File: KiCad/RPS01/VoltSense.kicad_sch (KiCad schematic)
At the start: 0 parts

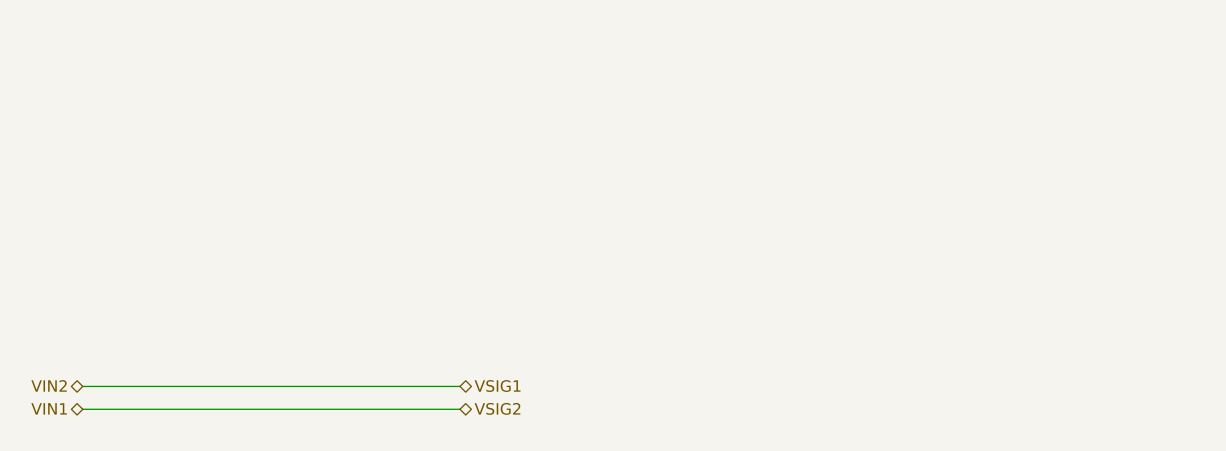
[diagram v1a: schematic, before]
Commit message: Finished most of the Schematics. Needs polishing
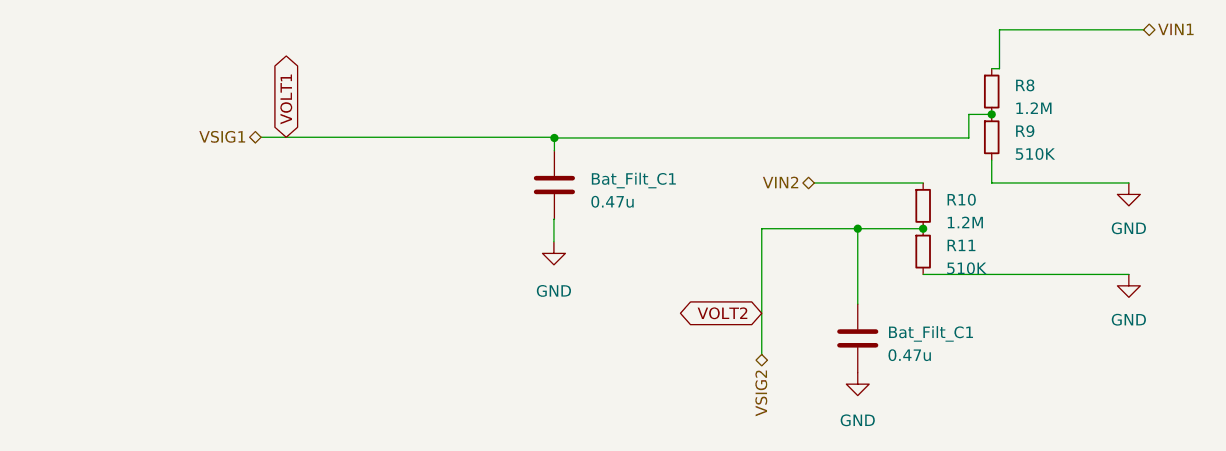
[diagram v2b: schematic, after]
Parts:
- added Bat_Filt_C1 (x2): 0.47u, symbol Device:C
- added R10, R8: 1.2M, Resistor_SMD:R_1206_3216Metric, symbol Device:R_Small
- added R11, R9: 510K, Resistor_SMD:R_1206_3216Metric, symbol Device:R_Small
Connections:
- net VIN1: now also R8.1
- net VIN2: now also R10.1
- new net GND: Bat_Filt_C1.2, Bat_Filt_C1.2, R11.2, R9.2
- new net VOLT1: Bat_Filt_C1.1, R8.2, R9.1
- new net VOLT2: Bat_Filt_C1.1, R10.2, R11.1

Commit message: Finished Updating Footprints and Reorganized Reference Designators
Finished Updating Footprints and Reorganized Reference Designators

Starting to work on Final PCB, except for 19V Boost. Please check Schematic for errors
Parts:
- Bat_Filt_C? (x2): renamed from Bat_Filt_C1; footprint (none) -> Capacitor_SMD:C_0603_1608Metric
- renumbered R9 to R?, R10 to R?, R8 to R?, R11 to R?
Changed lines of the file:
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@@
   (symbol (lib_id "Device:R_Small") (at 183.0324 49.784 0) (unit 1)
     (in_bom yes) (on_board yes) (dnp no) (fields_autoplaced)
-    (property "Reference" "R9" (at 185.5724 49.149 0)
+    (property "Reference" "R?" (at 185.5724 49.149 0)
       (effects (font (size 1.27 1.27)) (justify left))
     )
@@
       (project "rps01"
         (path "/14930f15-c0a0-4b55-93e6-b112548415f6/a2e49fe6-126d-427d-b045-54fb7f662aa7"
-          (reference "R9") (unit 1)
-        )
-        (path "/14930f15-c0a0-4b55-93e6-b112548415f6/86aa0a4b-8e23-451d-9b8a-c1446d1d5d38"
-          (reference "R23") (unit 1)
+          (reference "R?") (unit 1)
+        )
+        (path "/14930f15-c0a0-4b55-93e6-b112548415f6/86aa0a4b-8e23-451d-9b8a-c1446d1d5d38"
+          (reference "R28") (unit 1)
         )
       )
@@
   (symbol (lib_id "power:GND") (at 134.3914 61.4172 0) (unit 1)
     (in_bom yes) (on_board yes) (dnp no) (fields_autoplaced)
-    (property "Reference" "#PWR038" (at 134.3914 67.7672 0)
+    (property "Reference" "#PWR?" (at 134.3914 67.7672 0)
       (effects (font (size 1.27 1.27)) hide)
     )
@@
       (project "rps01"
         (path "/14930f15-c0a0-4b55-93e6-b112548415f6/a2e49fe6-126d-427d-b045-54fb7f662aa7"
-          (reference "#PWR038") (unit 1)
-        )
-        (path "/14930f15-c0a0-4b55-93e6-b112548415f6/86aa0a4b-8e23-451d-9b8a-c1446d1d5d38"
-          (reference "#PWR045") (unit 1)
+          (reference "#PWR?") (unit 1)
+        )
+        (path "/14930f15-c0a0-4b55-93e6-b112548415f6/86aa0a4b-8e23-451d-9b8a-c1446d1d5d38"
+          (reference "#PWR047") (unit 1)
         )
       )
@@
   (symbol (lib_id "power:GND") (at 168.148 75.946 0) (unit 1)
     (in_bom yes) (on_board yes) (dnp no) (fields_autoplaced)
-    (property "Reference" "#PWR046" (at 168.148 82.296 0)
+    (property "Reference" "#PWR048" (at 168.148 82.296 0)
       (effects (font (size 1.27 1.27)) hide)
     )
@@
       (project "rps01"
         (path "/14930f15-c0a0-4b55-93e6-b112548415f6/86aa0a4b-8e23-451d-9b8a-c1446d1d5d38"
-          (reference "#PWR046") (unit 1)
+          (reference "#PWR048") (unit 1)
         )
       )
@@
   (symbol (lib_id "Device:R_Small") (at 175.4124 57.404 0) (unit 1)
     (in_bom yes) (on_board yes) (dnp no) (fields_autoplaced)
-    (property "Reference" "R10" (at 177.9524 56.769 0)
+    (property "Reference" "R?" (at 177.9524 56.769 0)
       (effects (font (size 1.27 1.27)) (justify left))
     )
@@
       (project "rps01"
         (path "/14930f15-c0a0-4b55-93e6-b112548415f6/a2e49fe6-126d-427d-b045-54fb7f662aa7"
-          (reference "R10") (unit 1)
-        )
-        (path "/14930f15-c0a0-4b55-93e6-b112548415f6/86aa0a4b-8e23-451d-9b8a-c1446d1d5d38"
-          (reference "R20") (unit 1)
+          (reference "R?") (unit 1)
+        )
+        (path "/14930f15-c0a0-4b55-93e6-b112548415f6/86aa0a4b-8e23-451d-9b8a-c1446d1d5d38"
+          (reference "R25") (unit 1)
         )
       )
@@
   (symbol (lib_id "power:GND") (at 198.2724 54.864 0) (unit 1)
     (in_bom yes) (on_board yes) (dnp no) (fields_autoplaced)
-    (property "Reference" "#PWR019" (at 198.2724 61.214 0)
+    (property "Reference" "#PWR?" (at 198.2724 61.214 0)
       (effects (font (size 1.27 1.27)) hide)
     )
@@
       (project "rps01"
         (path "/14930f15-c0a0-4b55-93e6-b112548415f6/a2e49fe6-126d-427d-b045-54fb7f662aa7"
-          (reference "#PWR019") (unit 1)
-        )
-        (path "/14930f15-c0a0-4b55-93e6-b112548415f6/86aa0a4b-8e23-451d-9b8a-c1446d1d5d38"
-          (reference "#PWR047") (unit 1)
+          (reference "#PWR?") (unit 1)
+        )
+        (path "/14930f15-c0a0-4b55-93e6-b112548415f6/86aa0a4b-8e23-451d-9b8a-c1446d1d5d38"
+          (reference "#PWR049") (unit 1)
         )
       )
@@
   (symbol (lib_id "Device:C") (at 168.148 72.136 0) (unit 1)
     (in_bom yes) (on_board yes) (dnp no) (fields_autoplaced)
-    (property "Reference" "Bat_Filt_C1" (at 171.45 71.501 0)
+    (property "Reference" "Bat_Filt_C?" (at 171.45 71.501 0)
       (effects (font (size 1.27 1.27)) (justify left))
     )
@@
       (effects (font (size 1.27 1.27)) (justify left))
     )
-    (property "Footprint" "" (at 169.1132 75.946 0)
+    (property "Footprint" "Capacitor_SMD:C_0603_1608Metric" (at 169.1132 75.946 0)
       (effects (font (size 1.27 1.27)) hide)
     )
@@
       (project "rps01"
         (path "/14930f15-c0a0-4b55-93e6-b112548415f6/a2e49fe6-126d-427d-b045-54fb7f662aa7"
-          (reference "Bat_Filt_C1") (unit 1)
-        )
-        (path "/14930f15-c0a0-4b55-93e6-b112548415f6/86aa0a4b-8e23-451d-9b8a-c1446d1d5d38"
-          (reference "C9") (unit 1)
+          (reference "Bat_Filt_C?") (unit 1)
+        )
+        (path "/14930f15-c0a0-4b55-93e6-b112548415f6/86aa0a4b-8e23-451d-9b8a-c1446d1d5d38"
+          (reference "C12") (unit 1)
         )
       )
@@
   (symbol (lib_id "Device:C") (at 134.4422 55.0926 0) (unit 1)
     (in_bom yes) (on_board yes) (dnp no) (fields_autoplaced)
-    (property "Reference" "Bat_Filt_C1" (at 138.43 54.4576 0)
+    (property "Reference" "Bat_Filt_C?" (at 138.43 54.4576 0)
       (effects (font (size 1.27 1.27)) (justify left))
     )
@@
       (effects (font (size 1.27 1.27)) (justify left))
     )
-    (property "Footprint" "" (at 135.4074 58.9026 0)
+    (property "Footprint" "Capacitor_SMD:C_0603_1608Metric" (at 135.4074 58.9026 0)
       (effects (font (size 1.27 1.27)) hide)
     )
@@
       (project "rps01"
         (path "/14930f15-c0a0-4b55-93e6-b112548415f6/a2e49fe6-126d-427d-b045-54fb7f662aa7"
-          (reference "Bat_Filt_C1") (unit 1)
-        )
-        (path "/14930f15-c0a0-4b55-93e6-b112548415f6/86aa0a4b-8e23-451d-9b8a-c1446d1d5d38"
-          (reference "C8") (unit 1)
+          (reference "Bat_Filt_C?") (unit 1)
+        )
+        (path "/14930f15-c0a0-4b55-93e6-b112548415f6/86aa0a4b-8e23-451d-9b8a-c1446d1d5d38"
+          (reference "C11") (unit 1)
         )
       )
@@
   (symbol (lib_id "power:GND") (at 198.2724 65.024 0) (unit 1)
     (in_bom yes) (on_board yes) (dnp no) (fields_autoplaced)
-    (property "Reference" "#PWR024" (at 198.2724 71.374 0)
+    (property "Reference" "#PWR?" (at 198.2724 71.374 0)
       (effects (font (size 1.27 1.27)) hide)
     )
@@
       (project "rps01"
         (path "/14930f15-c0a0-4b55-93e6-b112548415f6/a2e49fe6-126d-427d-b045-54fb7f662aa7"
-          (reference "#PWR024") (unit 1)
-        )
-        (path "/14930f15-c0a0-4b55-93e6-b112548415f6/86aa0a4b-8e23-451d-9b8a-c1446d1d5d38"
-          (reference "#PWR048") (unit 1)
+          (reference "#PWR?") (unit 1)
+        )
+        (path "/14930f15-c0a0-4b55-93e6-b112548415f6/86aa0a4b-8e23-451d-9b8a-c1446d1d5d38"
+          (reference "#PWR050") (unit 1)
         )
       )
@@
   (symbol (lib_id "Device:R_Small") (at 183.0324 44.704 0) (unit 1)
     (in_bom yes) (on_board yes) (dnp no) (fields_autoplaced)
-    (property "Reference" "R8" (at 185.5724 44.069 0)
+    (property "Reference" "R?" (at 185.5724 44.069 0)
       (effects (font (size 1.27 1.27)) (justify left))
     )
@@
       (project "rps01"
         (path "/14930f15-c0a0-4b55-93e6-b112548415f6/a2e49fe6-126d-427d-b045-54fb7f662aa7"
-          (reference "R8") (unit 1)
-        )
-        (path "/14930f15-c0a0-4b55-93e6-b112548415f6/86aa0a4b-8e23-451d-9b8a-c1446d1d5d38"
-          (reference "R22") (unit 1)
+          (reference "R?") (unit 1)
+        )
+        (path "/14930f15-c0a0-4b55-93e6-b112548415f6/86aa0a4b-8e23-451d-9b8a-c1446d1d5d38"
+          (reference "R27") (unit 1)
         )
       )
@@
   (symbol (lib_id "Device:R_Small") (at 175.4124 62.484 0) (unit 1)
     (in_bom yes) (on_board yes) (dnp no) (fields_autoplaced)
-    (property "Reference" "R11" (at 177.9524 61.849 0)
+    (property "Reference" "R?" (at 177.9524 61.849 0)
       (effects (font (size 1.27 1.27)) (justify left))
     )
@@
       (project "rps01"
         (path "/14930f15-c0a0-4b55-93e6-b112548415f6/a2e49fe6-126d-427d-b045-54fb7f662aa7"
-          (reference "R11") (unit 1)
-        )
-        (path "/14930f15-c0a0-4b55-93e6-b112548415f6/86aa0a4b-8e23-451d-9b8a-c1446d1d5d38"
-          (reference "R21") (unit 1)
-        )
-      )
+          (reference "R?") (unit 1)
+        )
+        (path "/14930f15-c0a0-4b55-93e6-b112548415f6/86aa0a4b-8e23-451d-9b8a-c1446d1d5d38"
+          (reference "R26") (unit 1)
+        )
+      )

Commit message: Board Ready For layout. Except for 19V Boost? CHECK vs SIM Please
Board Ready For layout. Except for 19V Boost? CHECK vs SIM Please
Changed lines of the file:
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@@
   (symbol (lib_id "Device:R_Small") (at 183.0324 49.784 0) (unit 1)
     (in_bom yes) (on_board yes) (dnp no) (fields_autoplaced)
-    (property "Reference" "R?" (at 185.5724 49.149 0)
-      (effects (font (size 1.27 1.27)) (justify left))
-    )
-    (property "Value" "510K" (at 185.5724 51.689 0)
+    (property "Reference" "R?" (at 185.42 49.149 0)
+      (effects (font (size 1.27 1.27)) (justify left))
+    )
+    (property "Value" "510K" (at 185.42 51.689 0)
       (effects (font (size 1.27 1.27)) (justify left))
     )
@@
         )
         (path "/14930f15-c0a0-4b55-93e6-b112548415f6/86aa0a4b-8e23-451d-9b8a-c1446d1d5d38"
-          (reference "R28") (unit 1)
+          (reference "R_P8") (unit 1)
         )
       )
@@
         )
         (path "/14930f15-c0a0-4b55-93e6-b112548415f6/86aa0a4b-8e23-451d-9b8a-c1446d1d5d38"
-          (reference "#PWR047") (unit 1)
+          (reference "#PWR073") (unit 1)
         )
       )
@@
   (symbol (lib_id "power:GND") (at 168.148 75.946 0) (unit 1)
     (in_bom yes) (on_board yes) (dnp no) (fields_autoplaced)
-    (property "Reference" "#PWR048" (at 168.148 82.296 0)
+    (property "Reference" "#PWR075" (at 168.148 82.296 0)
       (effects (font (size 1.27 1.27)) hide)
     )
@@
       (project "rps01"
         (path "/14930f15-c0a0-4b55-93e6-b112548415f6/86aa0a4b-8e23-451d-9b8a-c1446d1d5d38"
-          (reference "#PWR048") (unit 1)
+          (reference "#PWR075") (unit 1)
         )
       )
@@
   (symbol (lib_id "Device:R_Small") (at 175.4124 57.404 0) (unit 1)
     (in_bom yes) (on_board yes) (dnp no) (fields_autoplaced)
-    (property "Reference" "R?" (at 177.9524 56.769 0)
-      (effects (font (size 1.27 1.27)) (justify left))
-    )
-    (property "Value" "1.2M" (at 177.9524 59.309 0)
+    (property "Reference" "R?" (at 177.8 56.769 0)
+      (effects (font (size 1.27 1.27)) (justify left))
+    )
+    (property "Value" "1.2M" (at 177.8 59.309 0)
       (effects (font (size 1.27 1.27)) (justify left))
     )
@@
         )
         (path "/14930f15-c0a0-4b55-93e6-b112548415f6/86aa0a4b-8e23-451d-9b8a-c1446d1d5d38"
-          (reference "R25") (unit 1)
+          (reference "R_P9") (unit 1)
         )
       )
@@
         )
         (path "/14930f15-c0a0-4b55-93e6-b112548415f6/86aa0a4b-8e23-451d-9b8a-c1446d1d5d38"
-          (reference "#PWR049") (unit 1)
+          (reference "#PWR072") (unit 1)
         )
       )
@@
         )
         (path "/14930f15-c0a0-4b55-93e6-b112548415f6/86aa0a4b-8e23-451d-9b8a-c1446d1d5d38"
-          (reference "C12") (unit 1)
+          (reference "C21") (unit 1)
         )
       )
@@
         )
         (path "/14930f15-c0a0-4b55-93e6-b112548415f6/86aa0a4b-8e23-451d-9b8a-c1446d1d5d38"
-          (reference "C11") (unit 1)
+          (reference "C20") (unit 1)
         )
       )
@@
         )
         (path "/14930f15-c0a0-4b55-93e6-b112548415f6/86aa0a4b-8e23-451d-9b8a-c1446d1d5d38"
-          (reference "#PWR050") (unit 1)
+          (reference "#PWR074") (unit 1)
         )
       )
@@
   (symbol (lib_id "Device:R_Small") (at 183.0324 44.704 0) (unit 1)
     (in_bom yes) (on_board yes) (dnp no) (fields_autoplaced)
-    (property "Reference" "R?" (at 185.5724 44.069 0)
-      (effects (font (size 1.27 1.27)) (justify left))
-    )
-    (property "Value" "1.2M" (at 185.5724 46.609 0)
+    (property "Reference" "R?" (at 185.42 44.069 0)
+      (effects (font (size 1.27 1.27)) (justify left))
+    )
+    (property "Value" "1.2M" (at 185.42 46.609 0)
       (effects (font (size 1.27 1.27)) (justify left))
     )
@@
         )
         (path "/14930f15-c0a0-4b55-93e6-b112548415f6/86aa0a4b-8e23-451d-9b8a-c1446d1d5d38"
-          (reference "R27") (unit 1)
+          (reference "R_P7") (unit 1)
         )
       )
@@
   (symbol (lib_id "Device:R_Small") (at 175.4124 62.484 0) (unit 1)
     (in_bom yes) (on_board yes) (dnp no) (fields_autoplaced)
-    (property "Reference" "R?" (at 177.9524 61.849 0)
-      (effects (font (size 1.27 1.27)) (justify left))
-    )
-    (property "Value" "510K" (at 177.9524 64.389 0)
+    (property "Reference" "R?" (at 177.8 61.849 0)
+      (effects (font (size 1.27 1.27)) (justify left))
+    )
+    (property "Value" "510K" (at 177.8 64.389 0)
       (effects (font (size 1.27 1.27)) (justify left))
     )
@@
         )
         (path "/14930f15-c0a0-4b55-93e6-b112548415f6/86aa0a4b-8e23-451d-9b8a-c1446d1d5d38"
-          (reference "R26") (unit 1)
-        )
-      )
+          (reference "R_P10") (unit 1)
+        )
+      )

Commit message: update cap and resistor values
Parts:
- Bat_Filt_C? (x2): value 0.47u -> 0.1u
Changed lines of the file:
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@@
       (effects (font (size 1.27 1.27)) (justify left))
     )
-    (property "Value" "0.47u" (at 171.45 74.041 0)
+    (property "Value" "0.1u" (at 171.45 74.041 0)
       (effects (font (size 1.27 1.27)) (justify left))
     )
@@
       (effects (font (size 1.27 1.27)) (justify left))
     )
-    (property "Value" "0.47u" (at 138.43 56.9976 0)
+    (property "Value" "0.1u" (at 138.43 56.9976 0)
       (effects (font (size 1.27 1.27)) (justify left))
     )
